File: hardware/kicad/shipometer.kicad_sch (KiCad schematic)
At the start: 26 parts, among them J101 Raspberry_Pi_40, J102 Conn_01x03, J104 ICM20948, J105 BME280, J106 ZED-F9R, U101 RaspberryPi 4B 2GB, U102 74LS138

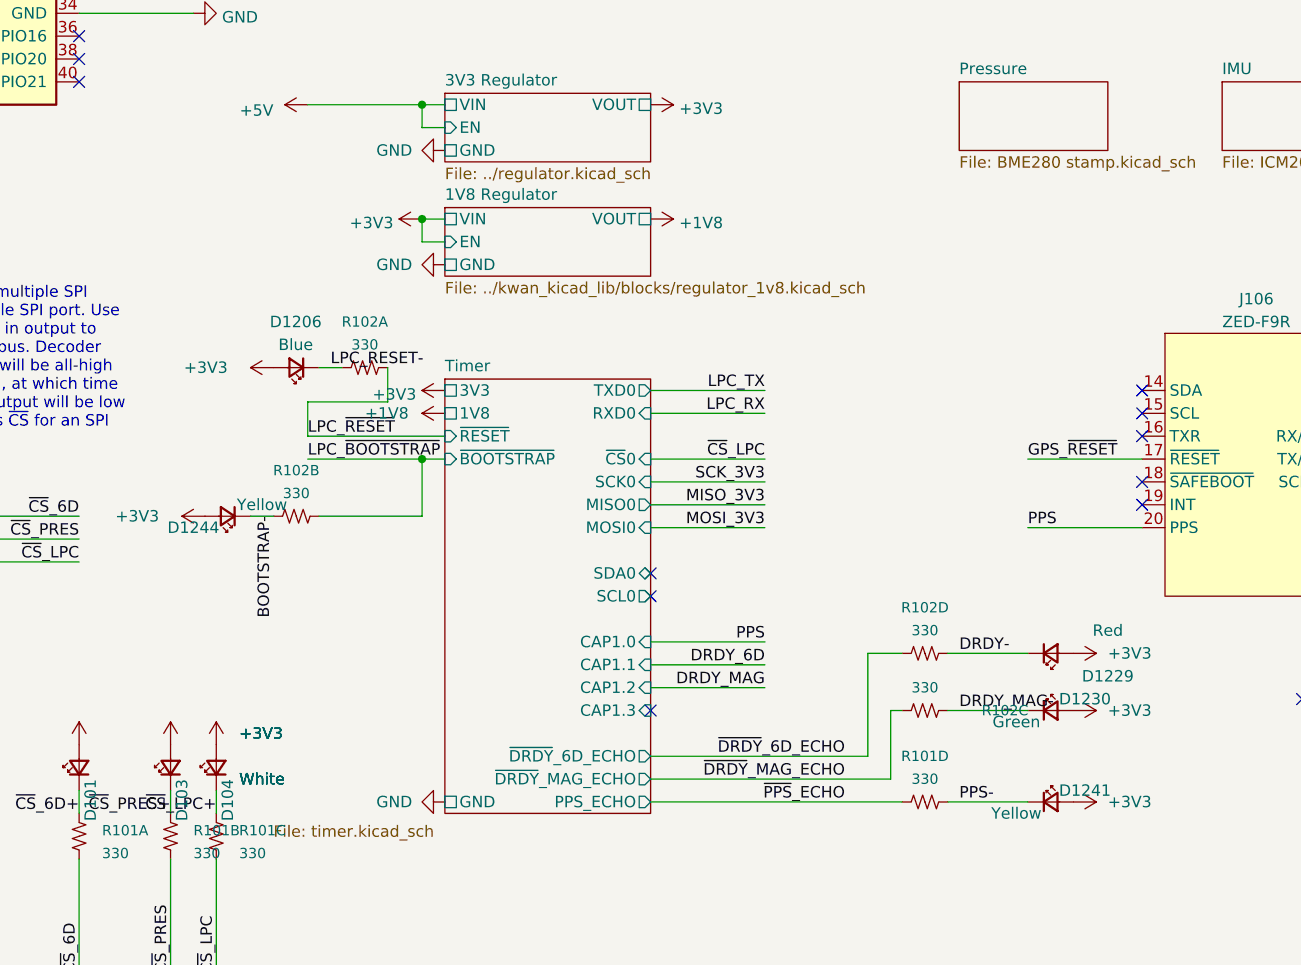
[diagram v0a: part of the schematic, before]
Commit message: Imported shipometer hat 23.04 as built, updated to Kicad 9
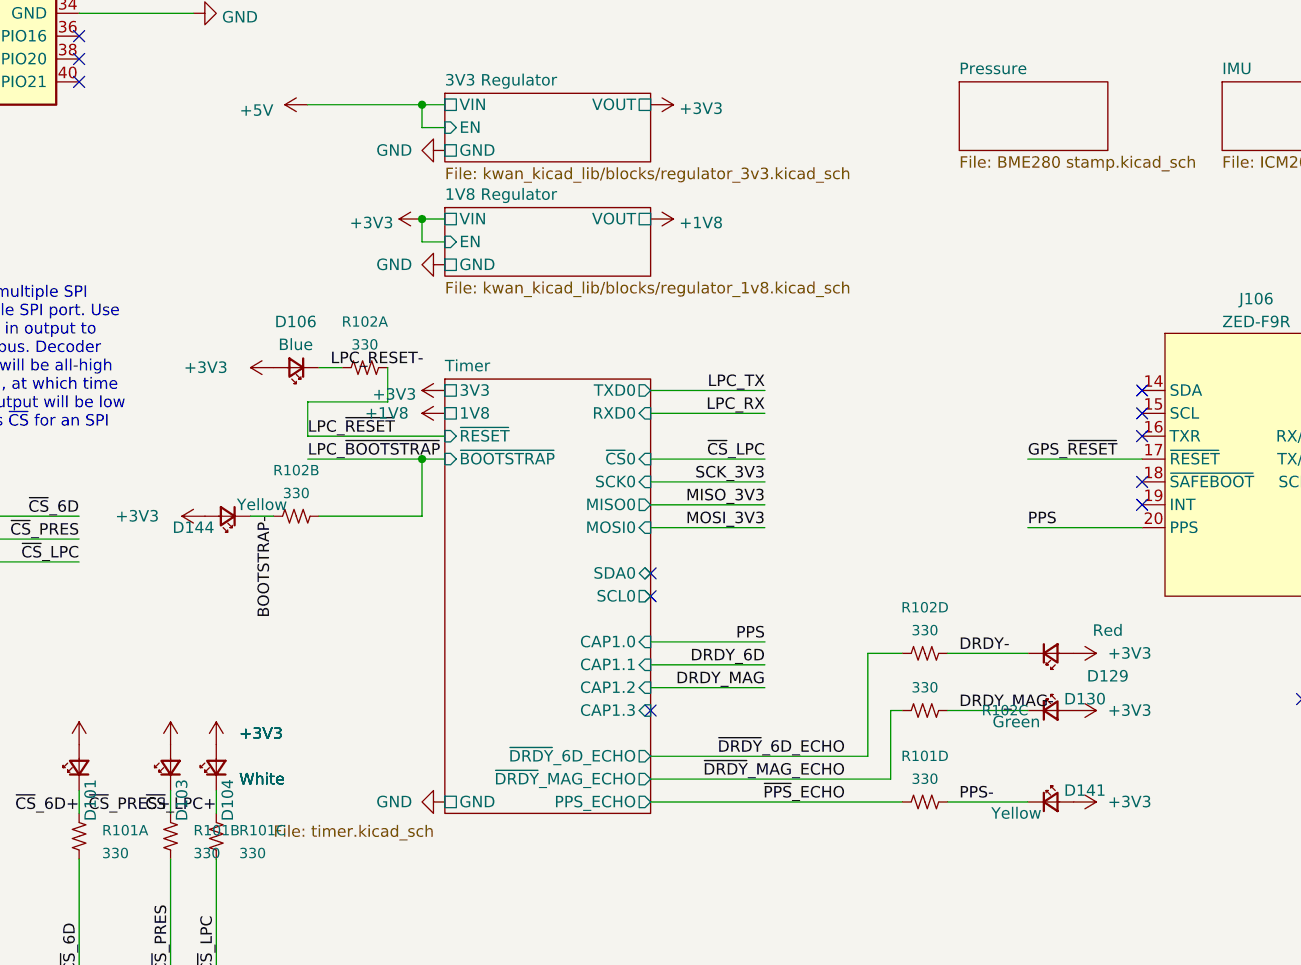
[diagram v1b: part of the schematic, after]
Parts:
- renumbered D1206 to D106, D1229 to D129, D1230 to D130, D1241 to D141, D1244 to D144
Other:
- sheet 1V8 Regulator: file ../kwan_kicad_lib/blocks/regulator_1v8.kicad_sch -> kwan_kicad_lib/blocks/regulator_1v8.kicad_sch
- sheet 3V3 Regulator: file ../regulator.kicad_sch -> kwan_kicad_lib/blocks/regulator_3v3.kicad_sch
